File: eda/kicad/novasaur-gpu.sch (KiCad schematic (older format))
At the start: 24 parts, among them U1 74F86, U28 74F163, U29 74F163, U3 74F11, U30 74F541, U31 74F574, U32 74F574, U33 74F541, U34 74F574, U35 74F299, U36 74F574, U37 74F157

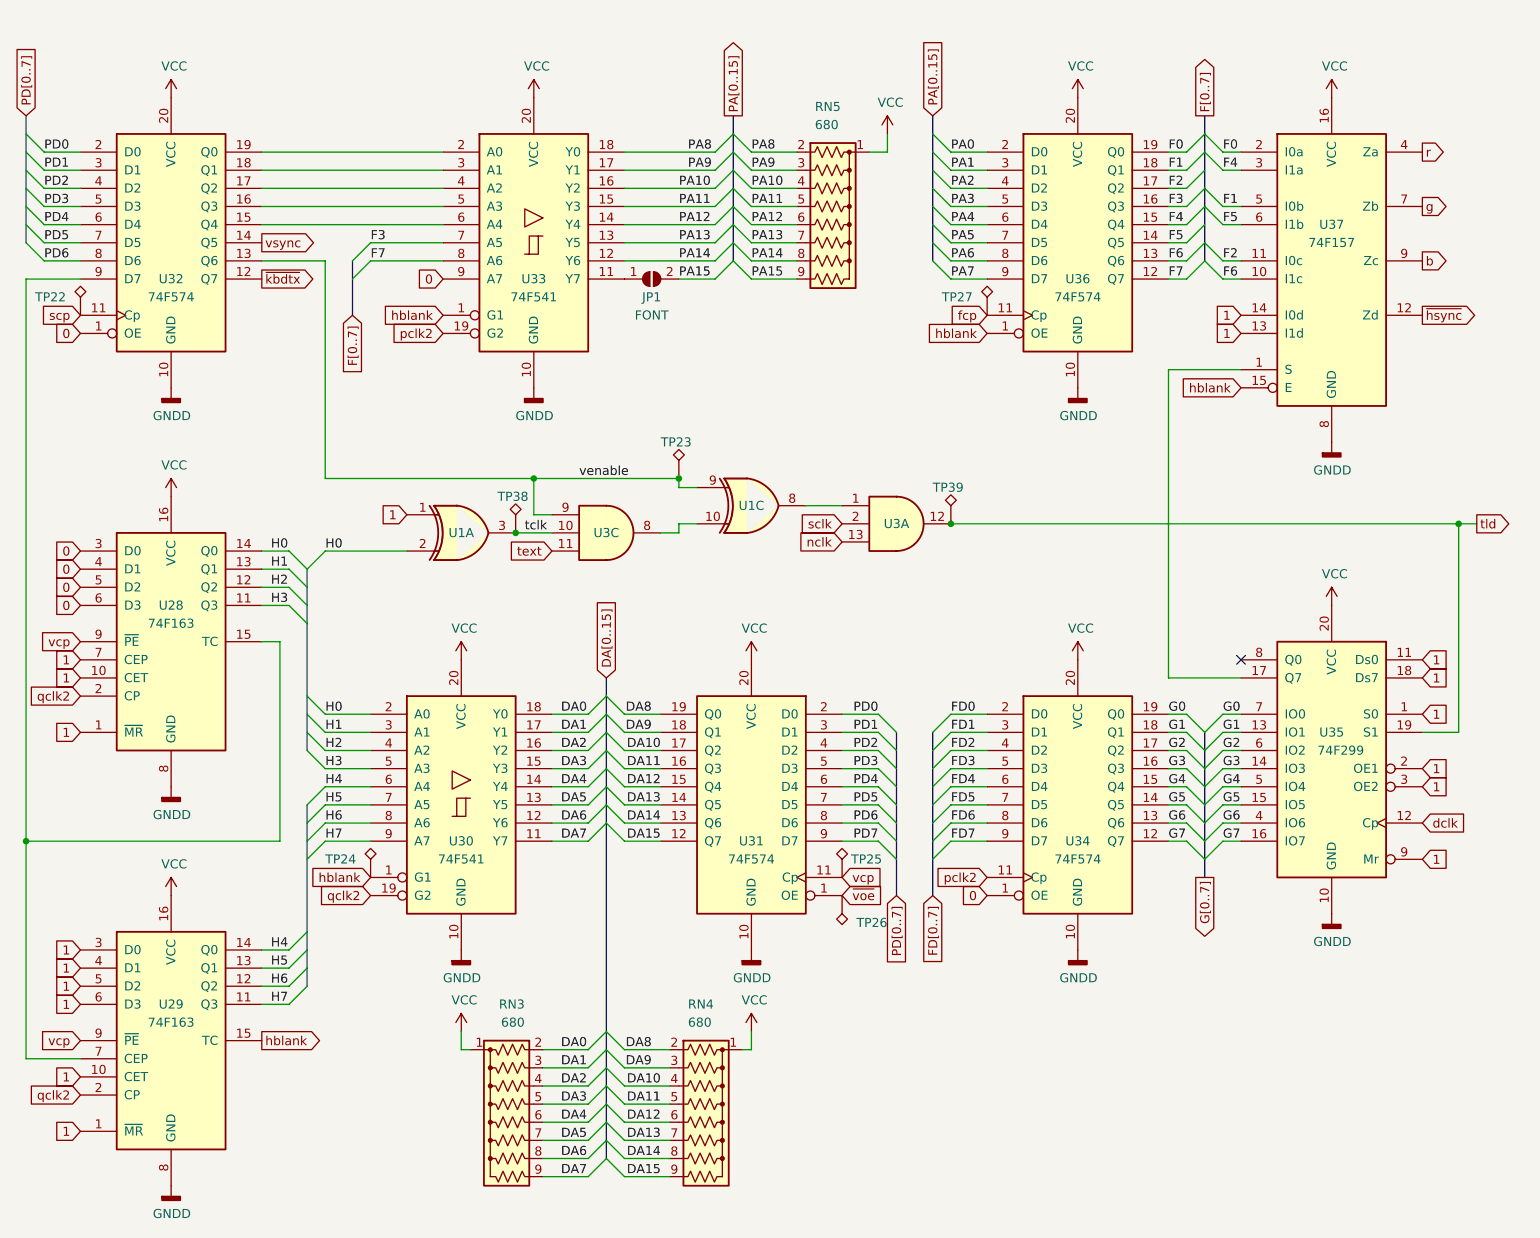
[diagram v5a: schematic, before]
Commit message: annotate registers
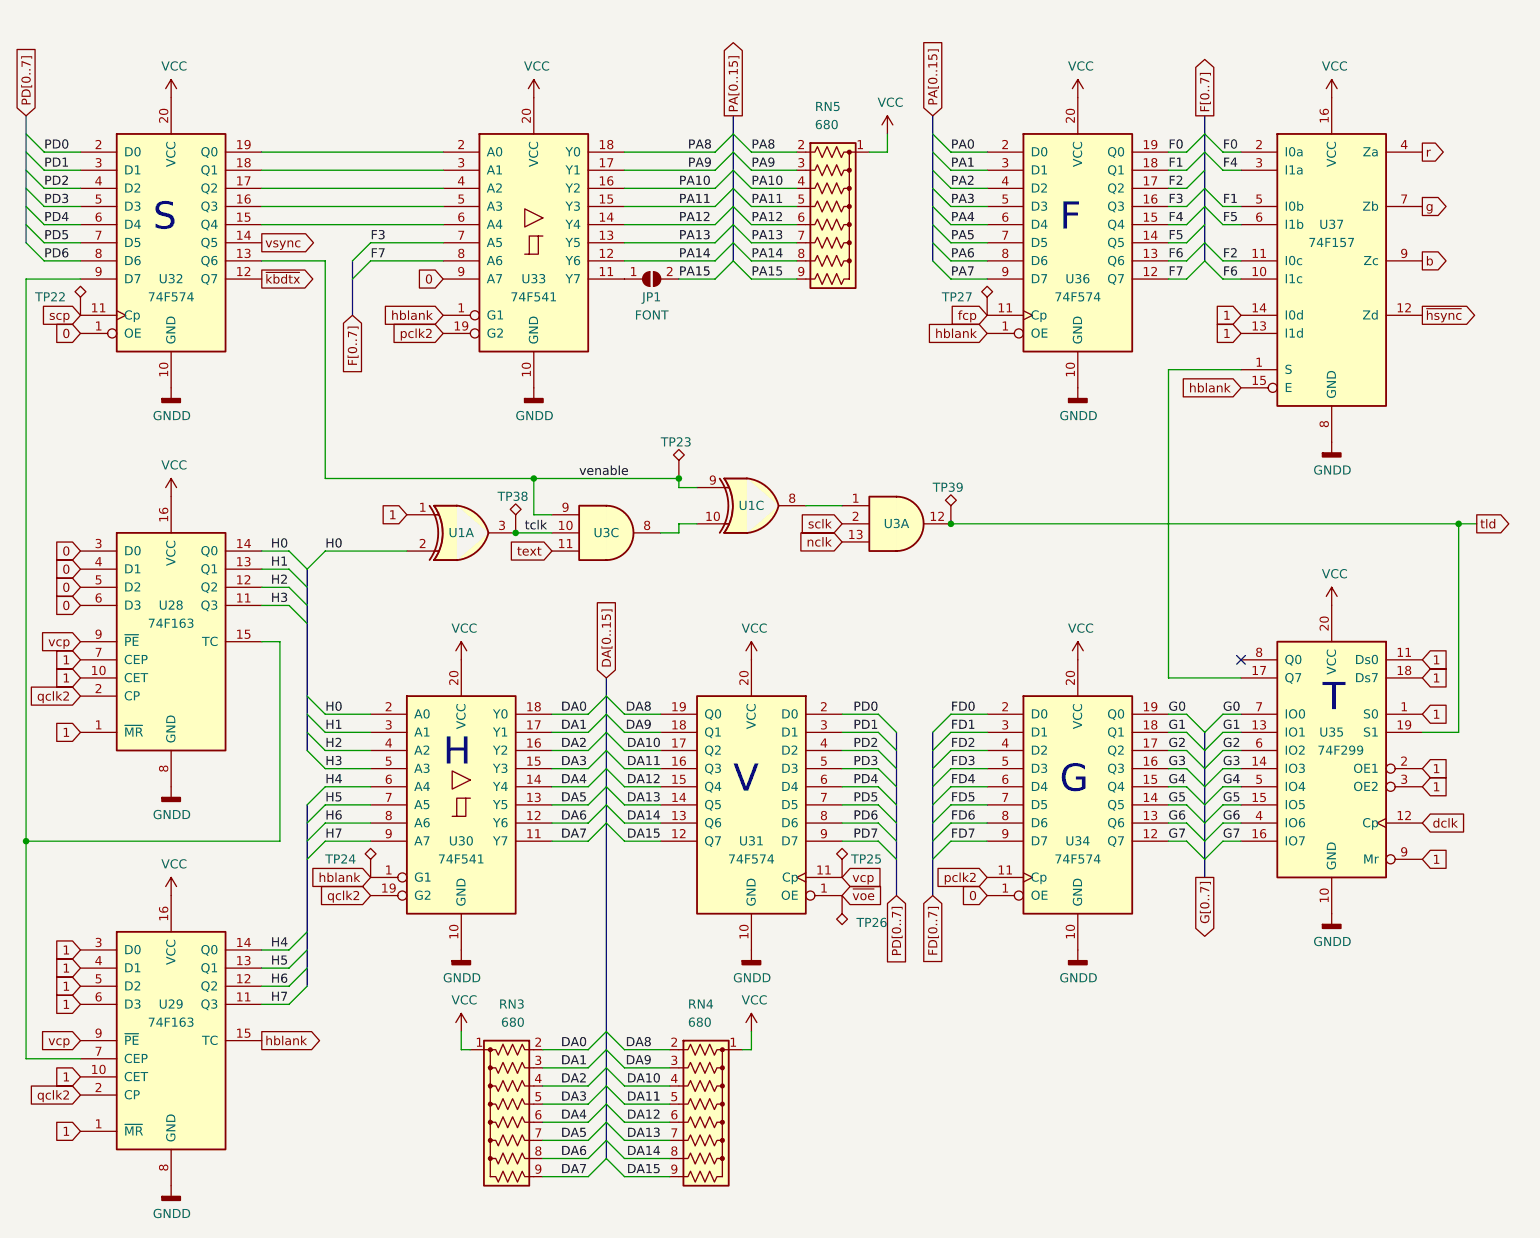
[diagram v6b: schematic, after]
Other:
- note added: "F"
- note added: "G"
- note added: "H"
- note added: "S"
- note added: "T"
- note added: "V"
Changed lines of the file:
@@
 Sheet 3 4
 Title "Graphics Processing Unit"
-Date "2021-10-20"
+Date "2021-11-20"
 Rev "1.10"
 Comp ""
@@
 Wire Wire Line
 	4200 3350 5000 3350
+Text Notes 2100 2000 0    150  ~ 0
+S
+Text Notes 3700 4950 0    150  ~ 0
+H
+Text Notes 5300 5100 0    150  ~ 0
+V
+Text Notes 7100 5100 0    150  ~ 0
+G
+Text Notes 8550 4650 0    150  ~ 0
+T
+Text Notes 7100 2000 0    150  ~ 0
+F
 Wire Bus Line
 	3200 2150 3200 2450
